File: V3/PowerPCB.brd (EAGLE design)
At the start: 171.9 x 151.6 mm, 107 parts, among them CON2 PINHEAD_1X08-2.54-FEMALE, CON3 PINHEAD_1X08-2.54-FEMALE, CON4 PINHEAD_1X06-2.54-FEMALE, CON7 PINHEAD_1X06-2.54-FEMALE, IC1 TPS54560B, IC2 TPS54560B, IC3 TPS54560B, IC4 TPS54560B, IC5 INA169, J1 CONNECTION-7MM, M1 BATTERY_CON-XT30-RA, M2 BATTERY_CON-XT30-RA, M3 BATTERY_CON-XT30-RA, M4 BATTERY_CON-XT30-RA, M5 BATTERY_CON-XT30-RA, M6 BATTERY_CON-XT30-RA, M7 BATTERY_CON-XT30-RA, Q1 IRFR2407PBF, Q2 IRFR2407PBF, Q3 IRFR2407PBF

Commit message: updates for V3
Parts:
- removed CON2: PINHEAD_1X08-2.54-FEMALE, pinhead:1X08-PTH-2.54-FEMALE
- added C43, C56, C57: 47u, rc:C1206
- added C44, C54: 2.2u, rc:C1206
- added C58: 0.1u, rc:C0603
- added C62: 10n, rc:C0603
- added C87: 47p, rc:C0603
- added C88: 4700p, rc:C0603
- added CON1: PINHEAD_1X12-2.54-FEMALE, pinhead:1X12-PTH-2.54-FEMALE
- added D10: B560C, Diodes:DO-214AB(SMC)
- added IC10: TPS54260, dc-dc:MSOP10
- added L1: 3.3uH, power_inductors:IHLP-2020BZ-01
- added R25, R27: 143K, rc:R0603
- added R28: 10K, rc:R0603
- added R29: 18K, rc:R0603
- moved J1 48.0 mm to (-2.05, 39.3), turned to 270 degrees
- moved M7 27.6 mm to (-53.8, 13.6), turned to 60 degrees
- moved PAD1 16.4 mm to (-52.2, -3.75)
- moved B3L 16.4 mm to (-53.2, -16.3)
- moved PAD8 7.66 mm to (48.5, -26.1)
- moved PAD2 4.65 mm to (51.1, 38.6)
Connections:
- new net BOOT: C58.2, IC10.1
- new net N$20: C62.1, IC10.4
- new net N$38: C87.1, IC10.8, R29.2
- new net N$39: IC10.5, R25.2
- new net N$50: C88.1, R29.1
- new net PH: C58.1, D10.C, IC10.10, L1.P$1
- new net VDD_4V: C43.P$1, C56.P$1, C57.P$1, CON1.3, CON1.4, L1.P$2, R27.2
- new net VSENSE: IC10.7, R27.1, R28.2
- net 5VFMU: now also CON1.10, CON1.8, CON1.9; no longer CON2.4, CON2.5, CON2.6
- net BATT_CURRENT: now also CON1.12; no longer CON2.8
- net BATT_VOLTAGE: now also CON1.11; no longer CON2.7
- net GND: now also C43.P$2, C44.P$1, C54.P$1, C56.P$2, C57.P$2, C62.2, C87.2, C88.2, CON1.1, CON1.2, CON1.5, CON1.6, CON1.7, D10.A, IC10.9, IC10.EP, R25.1, R28.1; no longer CON2.1, CON2.2, CON2.3
- net VBAT: now also C44.P$2, C54.P$2, IC10.2
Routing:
- net VDD_4V: track 0.00 -> 19.7 mm, vias 0 -> 2
- net VBAT: track 81.7 -> 90.9 mm, vias 7 -> 9
- net VSENSE: track 0.00 -> 8.11 mm
- net N$38: track 0.00 -> 6.34 mm
- net N$20: track 0.00 -> 4.07 mm
- net N$39: track 0.00 -> 2.65 mm
- net GND: track 10.2 -> 12.6 mm, vias 100 -> 127
- net BOOT: track 0.00 -> 2.17 mm
- net N$50: track 0.00 -> 1.40 mm
- net PWRSW: track 65.8 -> 64.9 mm
- net 5VFMU: track 33.5 -> 32.9 mm
- added copper zone on layer 1, net PH
- added copper zone on layer 1, net VDD_4V
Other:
- board text removed: "5VFMU"

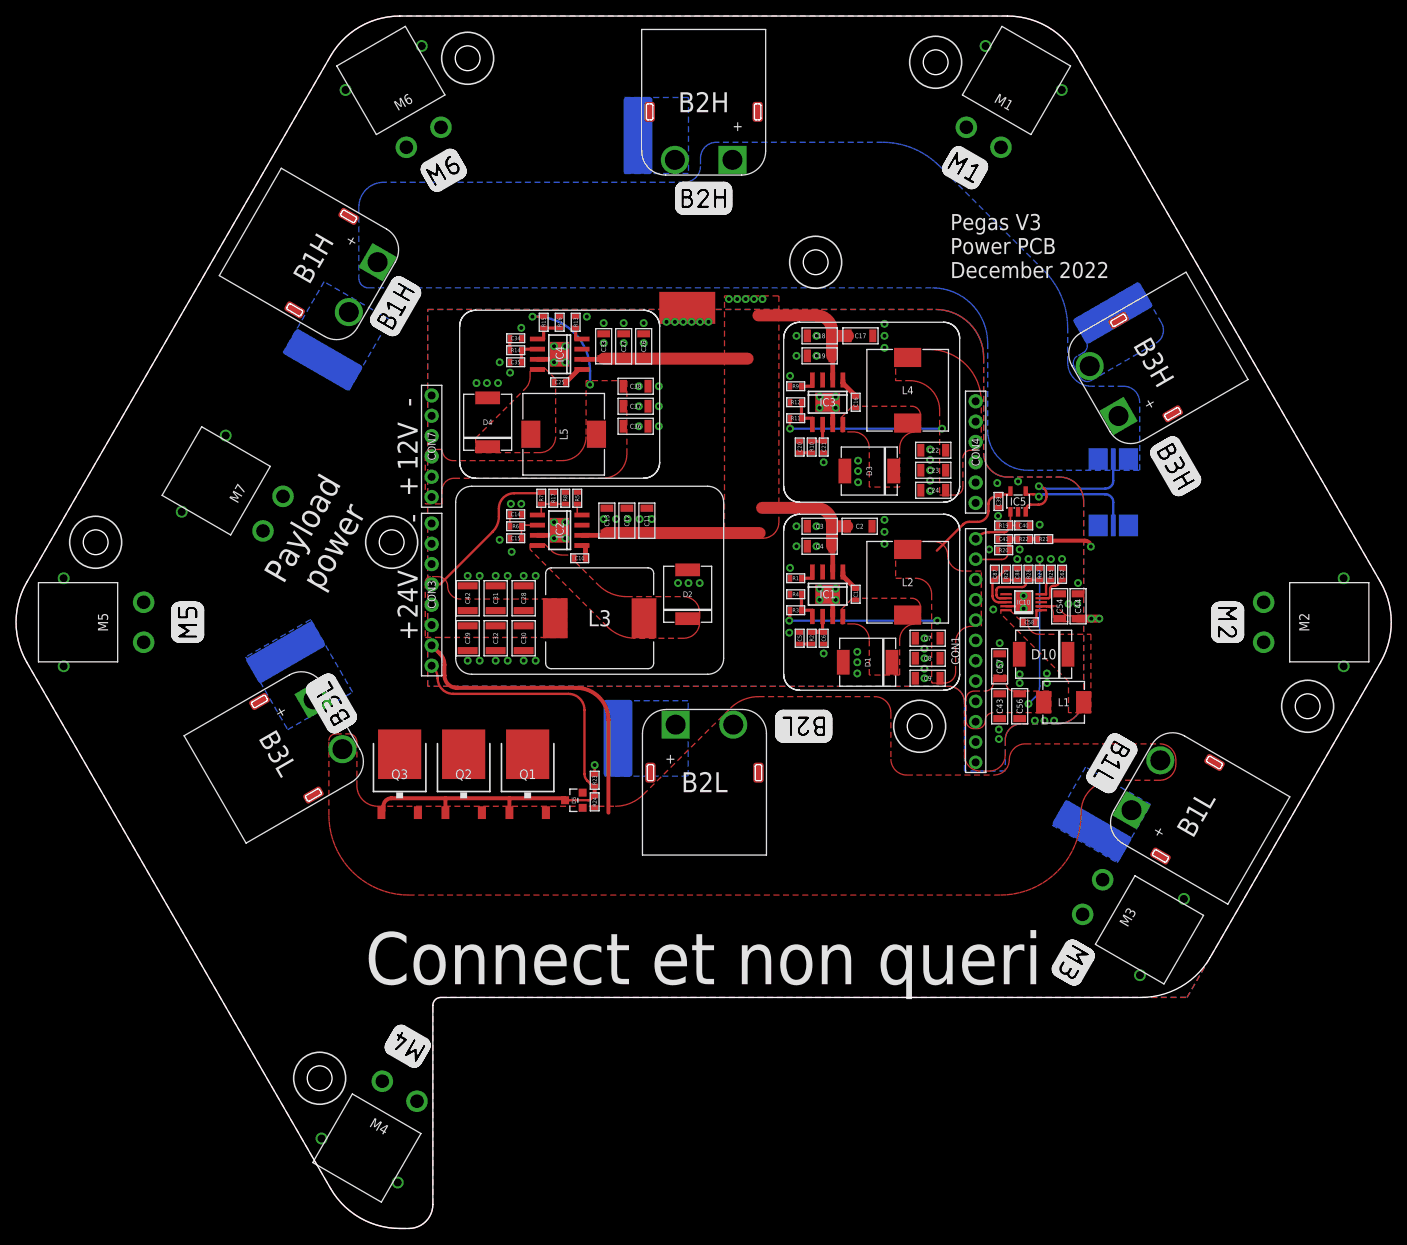
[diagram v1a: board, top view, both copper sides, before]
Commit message: silkscreen updates
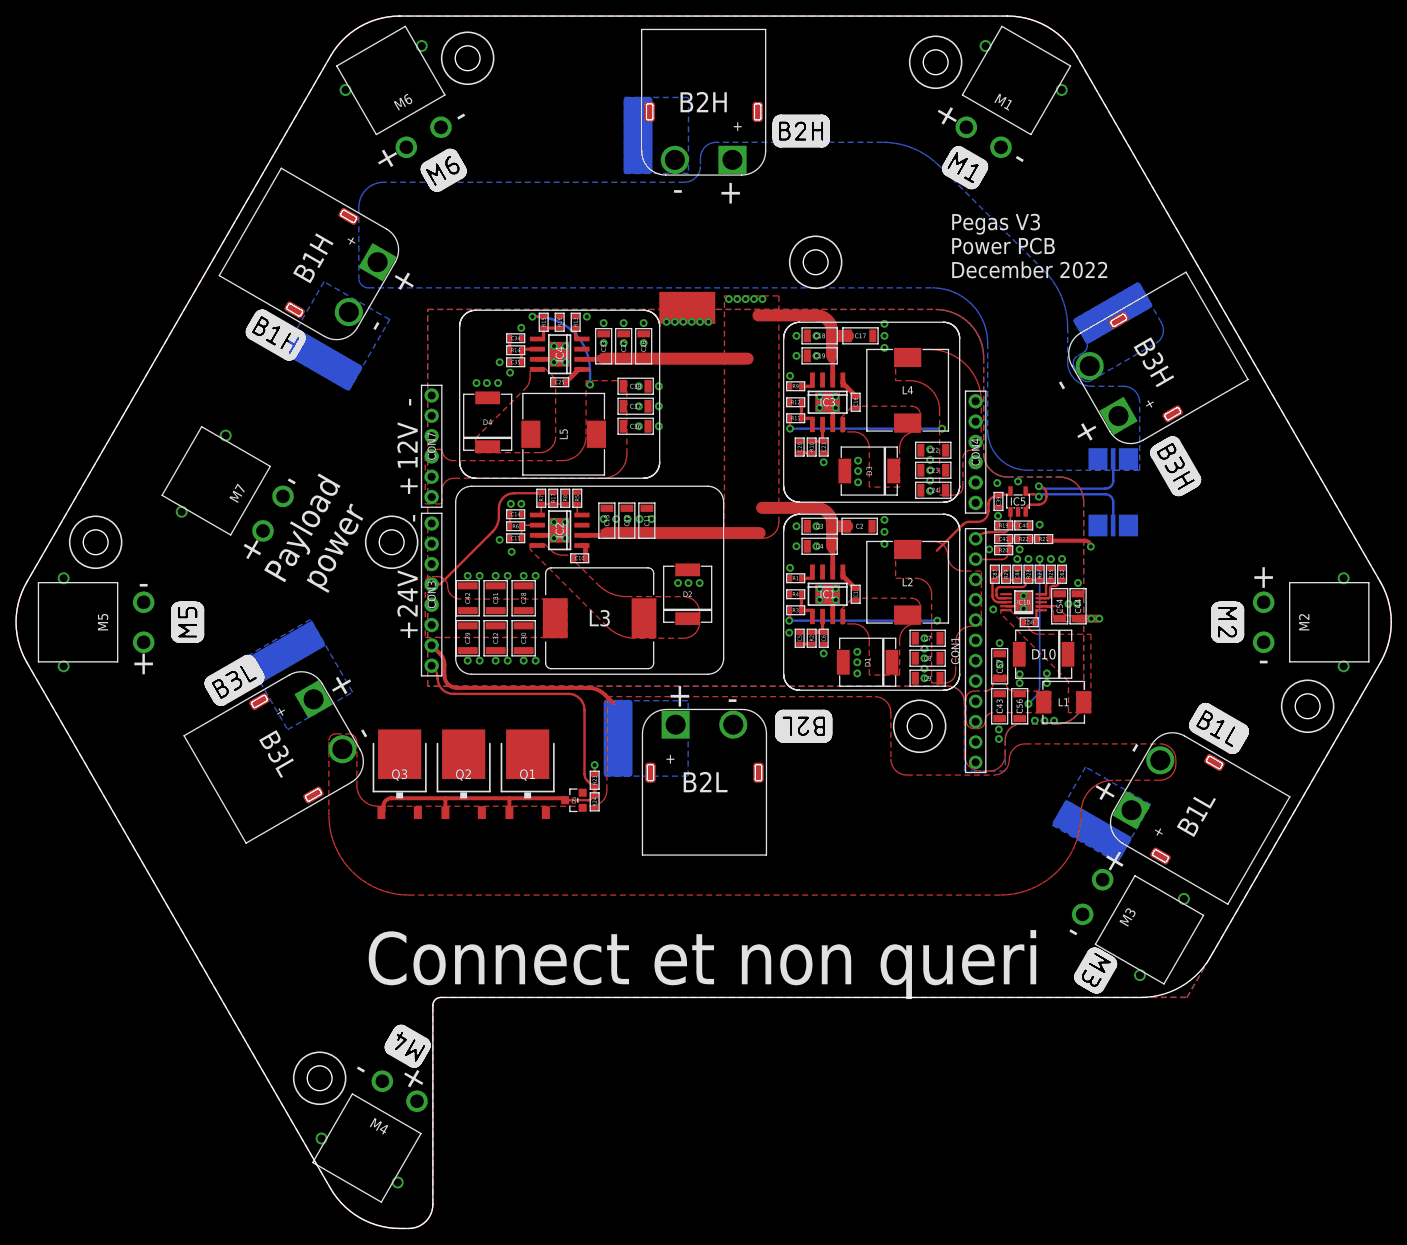
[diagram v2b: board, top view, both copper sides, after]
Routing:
- net BATNEG: track 38.7 -> 26.6 mm

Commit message: V3 finalization
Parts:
- added CON2: PINHEAD_1X06-2.54-FEMALE, pinhead:1X06-PTH-2.54-FEMALE
- CON3: value PINHEAD_1X08-2.54-FEMALE -> PINHEAD_1X02-2.54-FEMALE; device pinhead:1X08-PTH-2.54-FEMALE -> pinhead:1X02-PTH-2.54-FEMALE
- moved CON3 14.8 mm to (-23.5, -7.00), turned to 180 degrees
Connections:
- net BATNEG: now also CON3.1; no longer CON3.7
- net GND: now also CON2.1, CON2.2, CON2.3; no longer CON3.1, CON3.2, CON3.3
- net PWRSW: now also CON3.2; no longer CON3.8
- net VDD_24V: now also CON2.4, CON2.5, CON2.6; no longer CON3.4, CON3.5, CON3.6
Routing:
- net BATNEG: track 26.6 -> 12.1 mm
- net PWRSW: track 64.9 -> 54.4 mm
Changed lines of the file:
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@@
 <attribute name="VALUE" x="40" y="11.4" size="0.5" layer="27" font="vector" ratio="15" align="center"/>
-</element>
-<element name="CON3" library="pinhead" library_urn="urn:adsk.eagle:library:2540341" package="1X08-PTH-2.54-FEMALE" package3d_urn="urn:adsk.eagle:package:7747001/3" value="PINHEAD_1X08-2.54-FEMALE" x="-34" y="3.46" smashed="yes" rot="R270">
-<attribute name="NAME" x="-34" y="3.46" size="1" layer="25" font="vector" ratio="15" rot="R270" align="center"/>
 </element>
 <element name="R23" library="rc" library_urn="urn:adsk.eagle:library:2539423" package="R0603" package3d_urn="urn:adsk.eagle:package:2539454/3" value="10K2" x="-13.625" y="-19.75" smashed="yes" rot="R270">
@@
 <element name="CON1" library="pinhead" library_urn="urn:adsk.eagle:library:2540341" package="1X12-PTH-2.54-FEMALE" package3d_urn="urn:adsk.eagle:package:15583065/1" value="PINHEAD_1X12-2.54-FEMALE" x="34" y="-3.54" smashed="yes" rot="R90">
 <attribute name="NAME" x="31.46" y="-3.54" size="1" layer="25" font="vector" ratio="15" rot="R90" align="center"/>
+</element>
+<element name="CON2" library="pinhead" library_urn="urn:adsk.eagle:library:2540341" package="1X06-PTH-2.54-FEMALE" package3d_urn="urn:adsk.eagle:package:15321847/2" value="PINHEAD_1X06-2.54-FEMALE" x="-34" y="6" smashed="yes" rot="R270">
+<attribute name="NAME" x="-34" y="6" size="1" layer="25" font="vector" ratio="15" rot="R270" align="center"/>
+</element>
+<element name="CON3" library="pinhead" library_urn="urn:adsk.eagle:library:2540341" package="1X02-PTH-2.54-FEMALE" package3d_urn="urn:adsk.eagle:package:32579456/2" value="PINHEAD_1X02-2.54-FEMALE" x="-23.5" y="-7" smashed="yes" rot="R180">
+<attribute name="NAME" x="-23.5" y="-9" size="1" layer="25" font="vector" ratio="15" rot="R180" align="center"/>
 </element>
 </elements>
@@
 <contactref element="C41" pad="1"/>
 <contactref element="R20" pad="1"/>
-<contactref element="CON3" pad="1"/>
-<contactref element="CON3" pad="2"/>
-<contactref element="CON3" pad="3"/>
 <via x="36.8" y="13.3" extent="1-16" drill="0.5" diameter="1"/>
 <via x="35.7" y="9.1" extent="1-16" drill="0.5" diameter="1"/>
@@
 <via x="-0.45" y="37.55" extent="1-16" drill="0.5" diameter="1"/>
 <via x="0.6" y="37.55" extent="1-16" drill="0.5" diameter="1"/>
+<contactref element="CON2" pad="1"/>
+<contactref element="CON2" pad="2"/>
+<contactref element="CON2" pad="3"/>
 </signal>
 <signal name="VDD_5V">
@@
 <wire x1="-25.6" y1="13.2041625" x2="-26.3807625" y2="11.3192375" width="0.3" layer="1" curve="-45.000063"/>
 <wire x1="-26.3807625" y1="11.3192375" x2="-32.97" y2="4.73" width="0.3" layer="1"/>
-<contactref element="CON3" pad="4"/>
-<contactref element="CON3" pad="5"/>
-<contactref element="CON3" pad="6"/>
+<contactref element="CON2" pad="4"/>
+<contactref element="CON2" pad="5"/>
+<contactref element="CON2" pad="6"/>
 </signal>
 <signal name="BOOT1">
@@
 <contactref element="D5" pad="1"/>
 <contactref element="R24" pad="2"/>
-<contactref element="CON3" pad="7"/>
-<wire x1="-30.85" y1="-8.2" x2="-14.442640625" y2="-8.2" width="0.5" layer="1"/>
-<wire x1="-14.442640625" y1="-8.2" x2="-12.321321875" y2="-9.078678125" width="0.5" layer="1" curve="-44.999958"/>
-<wire x1="-12.321321875" y1="-9.078678125" x2="-11.3" y2="-10.1" width="0.5" layer="1"/>
-<wire x1="-30.85" y1="-8.2" x2="-32.4" y2="-6.65" width="0.5" layer="1" curve="-90"/>
-<wire x1="-32.4" y1="-6.65" x2="-32.4" y2="-5.318428125" width="0.5" layer="1"/>
-<wire x1="-32.4" y1="-5.318428125" x2="-32.9857875" y2="-3.9042125" width="0.5" layer="1" curve="45.000063"/>
-<wire x1="-32.9857875" y1="-3.9042125" x2="-34" y2="-2.89" width="0.5" layer="1"/>
+<contactref element="CON3" pad="1"/>
+<wire x1="-22.23" y1="-7" x2="-22.208678125" y2="-7.021321875" width="0.3" layer="1"/>
+<wire x1="-22.208678125" y1="-7.021321875" x2="-20.087359375" y2="-7.9" width="0.3" layer="1" curve="44.99994"/>
+<wire x1="-20.087359375" y1="-7.9" x2="-14.742640625" y2="-7.9" width="0.3" layer="1"/>
+<wire x1="-14.742640625" y1="-7.9" x2="-12.621321875" y2="-8.778678125" width="0.3" layer="1" curve="-44.999958"/>
+<wire x1="-12.621321875" y1="-8.778678125" x2="-11.1" y2="-10.3" width="0.3" layer="1"/>
 </signal>
 <signal name="PWRSW">
@@
 <contactref element="D5" pad="3"/>
 <contactref element="R24" pad="1"/>
-<contactref element="CON3" pad="8"/>
 <wire x1="-40.03" y1="-23.55" x2="-40.03" y2="-23" width="0.5" layer="1"/>
 <wire x1="-40.03" y1="-23" x2="-39.03" y2="-22" width="0.5" layer="1" curve="-90"/>
@@
 <wire x1="-14.425" y1="-22.25" x2="-17.325" y2="-22.25" width="0.3" layer="1"/>
 <wire x1="-13.925" y1="-21.725" x2="-13.625" y2="-21.725" width="0.3" layer="1"/>
-<wire x1="-34" y1="-5.43" x2="-33.8357875" y2="-5.5942125" width="0.3" layer="1"/>
-<wire x1="-33.8357875" y1="-5.5942125" x2="-33.25" y2="-7.008428125" width="0.3" layer="1" curve="-45.00009"/>
-<wire x1="-33.25" y1="-7.008428125" x2="-31.308428125" y2="-8.95" width="0.3" layer="1" curve="90"/>
-<wire x1="-31.308428125" y1="-8.95" x2="-16.9" y2="-8.95" width="0.3" layer="1"/>
-<wire x1="-16.9" y1="-8.95" x2="-14.9" y2="-10.95" width="0.3" layer="1" curve="-90"/>
-<wire x1="-14.9" y1="-10.95" x2="-14.9" y2="-18.94228125" width="0.3" layer="1"/>
-<wire x1="-14.9" y1="-18.94228125" x2="-14.540990625" y2="-19.809009375" width="0.3" layer="1" curve="45.000063"/>
-<wire x1="-14.540990625" y1="-19.809009375" x2="-13.875" y2="-20.475" width="0.3" layer="1"/>
+<wire x1="-14.9" y1="-10.95" x2="-16.9" y2="-8.95" width="0.3" layer="1" curve="90"/>
+<wire x1="-14.9" y1="-10.95" x2="-14.9" y2="-18.207359375" width="0.3" layer="1"/>
+<wire x1="-14.9" y1="-18.207359375" x2="-14.021321875" y2="-20.328678125" width="0.3" layer="1" curve="44.999958"/>
+<wire x1="-14.021321875" y1="-20.328678125" x2="-13.875" y2="-20.475" width="0.3" layer="1"/>
 <wire x1="-13.875" y1="-20.475" x2="-13.625" y2="-20.475" width="0.3" layer="1"/>
+<contactref element="CON3" pad="2"/>
+<wire x1="-16.9" y1="-8.95" x2="-21.577359375" y2="-8.95" width="0.3" layer="1"/>
+<wire x1="-21.577359375" y1="-8.95" x2="-23.698678125" y2="-8.071321875" width="0.3" layer="1" curve="-44.999958"/>
+<wire x1="-23.698678125" y1="-8.071321875" x2="-24.77" y2="-7" width="0.3" layer="1"/>
 </signal>
 <signal name="BATT_VOLTAGE">
